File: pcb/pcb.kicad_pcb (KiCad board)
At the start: 2 copper layers, 75 x 50 mm, 104 parts, among them J1 I2C, J2 HR911105A, J3 USB_C_Receptacle_USB2.0, J4 GPS, J5 DNP, Q1 BC817, Q2 WPM2015-3_TR, Q3 BC817, Q4 BC817, Q5 BC817, SW1 DNP, SW2 DNP, U1 ESP32-WROOM-32D, U2 LAN8710A, U3 ADXL355, U4 MIC5219-3.3YM5, U5 74LVC1G17, U6 CP2102N-A01-GQFN24

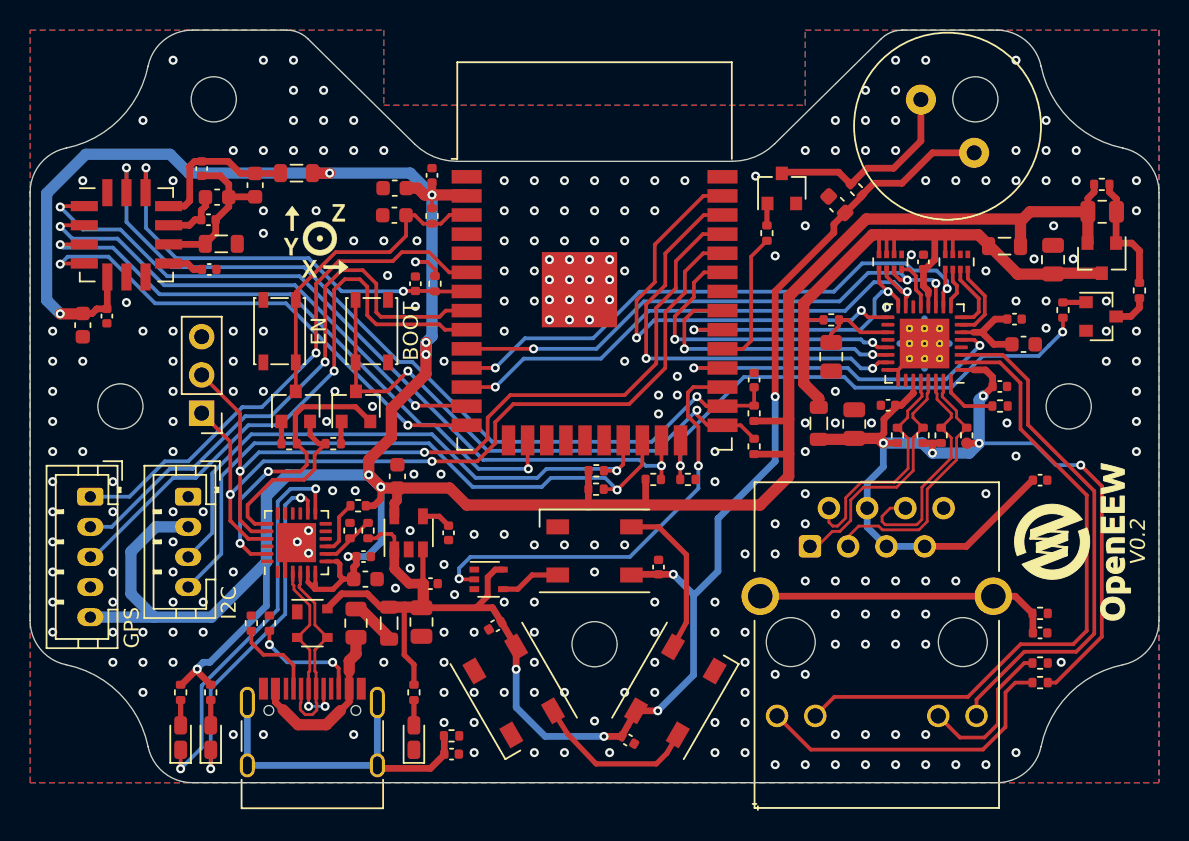
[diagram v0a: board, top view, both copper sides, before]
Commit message: KiCAD5.1.9: replaced CP2102N schematic symbol
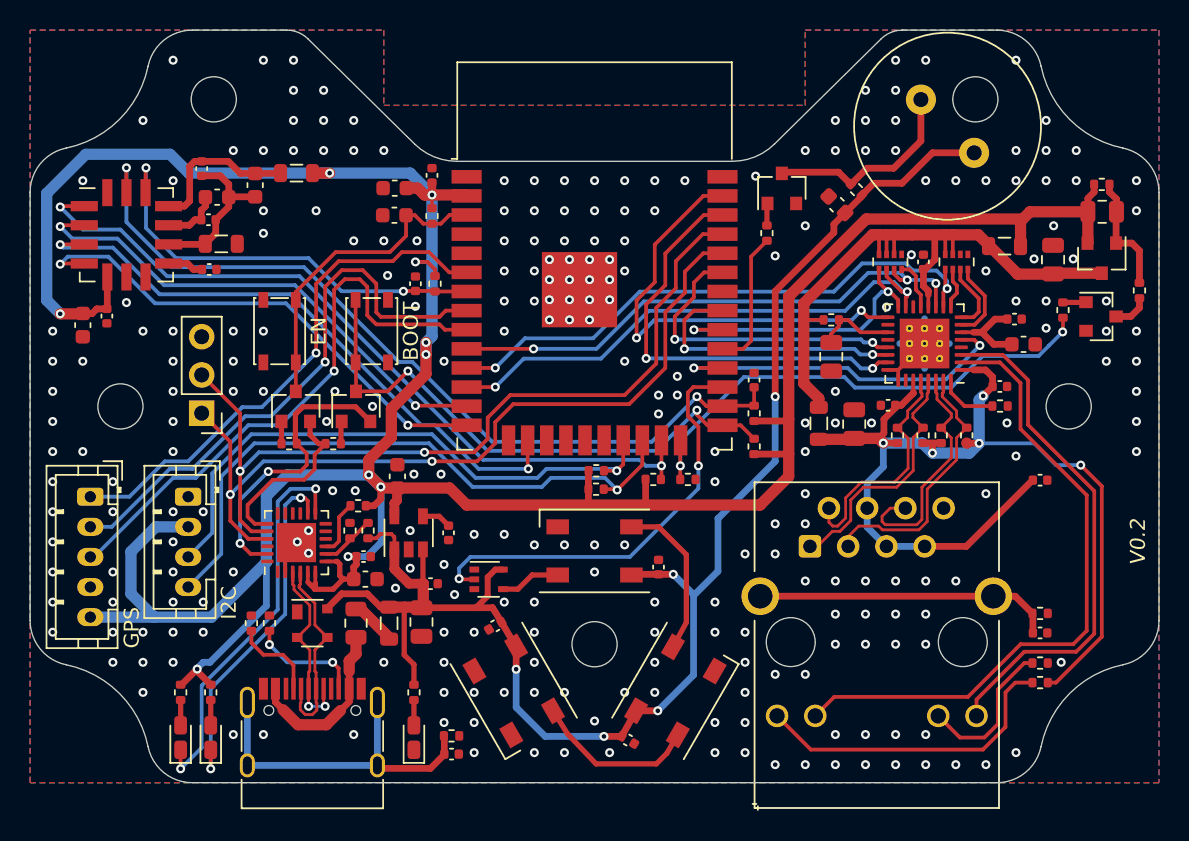
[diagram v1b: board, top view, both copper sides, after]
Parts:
- removed REF**: Text_OpenEEW_2mm, Symbol_local:Text_OpenEEW_2mm
- removed REF**: Logo_OpenEEW_5mm, Symbol_local:Logo_OpenEEW_5mm
- removed REF**: Accelerometer_Orientation_5mm, Symbol_local:Accelerometer_Orientation_5mm
- R14: value 510 -> 1k
- U6: value CP2102N-A01-GQFN24 -> CP2102N-Axx-xQFN24
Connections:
- D3 pad 2: Net-(D3-Pad2) -> (no net)
- J3 pad A8: Net-(J3-PadA8) -> (no net)
- J3 pad B8: Net-(J3-PadB8) -> (no net)
- U1 pad 17: Net-(U1-Pad17) -> (no net)
- U1 pad 18: Net-(U1-Pad18) -> (no net)
- U1 pad 19: Net-(U1-Pad19) -> (no net)
- U1 pad 20: Net-(U1-Pad20) -> (no net)
- U1 pad 32: Net-(U1-Pad32) -> (no net)
- U1 pad 4: Net-(U1-Pad4) -> (no net)
- U1 pad 5: Net-(U1-Pad5) -> (no net)
- U2 pad 14: Net-(U2-Pad14) -> (no net)
- U2 pad 18: Net-(U2-Pad18) -> (no net)
- U2 pad 20: Net-(U2-Pad20) -> (no net)
- U2 pad 26: Net-(U2-Pad26) -> (no net)
- U2 pad 4: Net-(U2-Pad4) -> (no net)
- U3 pad 14: Net-(U3-Pad14) -> (no net)
- U3 pad 7: Net-(U3-Pad7) -> (no net)
- U6 pad 1: Net-(U6-Pad1) -> (no net)
- U6 pad 10: Net-(U6-Pad10) -> (no net)
- U6 pad 11: Net-(U6-Pad11) -> (no net)
- U6 pad 12: Net-(U6-Pad12) -> (no net)
- U6 pad 15: Net-(U6-Pad15) -> (no net)
- U6 pad 16: Net-(U6-Pad16) -> (no net)
- U6 pad 17: Net-(U6-Pad17) -> (no net)
- U6 pad 18: Net-(U6-Pad18) -> (no net)
- U6 pad 22: Net-(U6-Pad22) -> (no net)
- U6 pad 24: Net-(U6-Pad24) -> (no net)
